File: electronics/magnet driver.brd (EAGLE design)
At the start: 101.6 x 101.6 mm, 23 parts, among them J1 1-770968-0, J2 DF1BZ-8DP-2.5DSA, K1 G2RL-2DC12, Q1 RK7002BMT116, Q2 DMN1019UVT-7DMN1019UVT-7, Q3 PMBT2222A,215PMBT2222A,215, U1 ATMEGA328PB32-TQFP

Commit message: Added pull-up on RESET
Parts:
- added R1: 10k, Zach:0805
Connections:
- net !RESET: now also R1.P$1
- net +3V3: now also R1.P$2
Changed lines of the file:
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@@
 <attribute name="NAME" x="-43.18" y="57.5936" size="0.8128" layer="25" align="bottom-center"/>
+</element>
+<element name="R1" library="Zach" package="0805" value="10k" x="-59.69" y="-2.54" smashed="yes">
+<attribute name="NAME" x="-59.69" y="-1.6764" size="0.8128" layer="25" align="bottom-center"/>
 </element>
 </elements>
@@
 <contactref element="J1" pad="3"/>
 <contactref element="J2" pad="1"/>
-<wire x1="-25.7175" y1="68.58" x2="-21.9075" y2="68.58" width="0" layer="19" extent="1-1"/>
-<wire x1="-29.5275" y1="68.58" x2="-25.7175" y2="68.58" width="0" layer="19" extent="1-1"/>
+<contactref element="R1" pad="P$2"/>
+<wire x1="-53.81" y1="13.94" x2="-58.7375" y2="-2.54" width="0" layer="19" extent="1-1"/>
+<wire x1="-53.28" y1="45.7" x2="-53.81" y2="13.94" width="0" layer="19" extent="1-1"/>
+<wire x1="-40.2045" y1="56.855" x2="-53.28" y2="45.7" width="0" layer="19" extent="1-1"/>
+<wire x1="-44.7675" y1="68.58" x2="-40.2045" y2="56.855" width="0" layer="19" extent="1-1"/>
+<wire x1="-29.5275" y1="68.58" x2="-44.7675" y2="68.58" width="0" layer="19" extent="1-1"/>
+<wire x1="-25.7175" y1="68.58" x2="-29.5275" y2="68.58" width="0" layer="19" extent="1-1"/>
+<wire x1="-21.9075" y1="68.58" x2="-25.7175" y2="68.58" width="0" layer="19" extent="1-1"/>
 <wire x1="-21.9513" y1="60.09" x2="-21.9075" y2="68.58" width="0" layer="19" extent="1-1"/>
 <wire x1="-13.6087" y1="59.29" x2="-21.9513" y2="60.09" width="0" layer="19" extent="1-1"/>
 <wire x1="-13.6087" y1="57.69" x2="-13.6087" y2="59.29" width="0" layer="19" extent="1-1"/>
-<wire x1="-44.7675" y1="68.58" x2="-29.5275" y2="68.58" width="0" layer="19" extent="1-1"/>
-<wire x1="-40.2045" y1="56.855" x2="-44.7675" y2="68.58" width="0" layer="19" extent="1-1"/>
-<wire x1="-53.28" y1="45.7" x2="-40.2045" y2="56.855" width="0" layer="19" extent="1-1"/>
-<wire x1="-53.81" y1="13.94" x2="-53.28" y2="45.7" width="0" layer="19" extent="1-1"/>
 </signal>
 <signal name="U/!D">
@@
 <contactref element="J2" pad="2"/>
 <contactref element="U1" pad="29"/>
-<wire x1="-50.78" y1="45.7" x2="-18.18" y2="63.8613" width="0" layer="19" extent="1-1"/>
+<contactref element="R1" pad="P$1"/>
+<wire x1="-50.78" y1="45.7" x2="-60.6425" y2="-2.54" width="0" layer="19" extent="1-1"/>
+<wire x1="-18.18" y1="63.8613" x2="-50.78" y2="45.7" width="0" layer="19" extent="1-1"/>
 </signal>
 <signal name="XTAL2">

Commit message: Update magnet driver.brd
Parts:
- added J3: 1-770969-0, Zach:1-770969-0
- moved J1 161.4 mm to (101.6, 36.6), turned to 90 degrees
- moved R1 131.3 mm to (64.3, 40.9), turned to 180 degrees
- moved J2 112.6 mm to (63.0, 48.3), turned to 270 degrees
- moved D2 103.9 mm to (46.2, 66.3)
- moved XTAL1 97.6 mm to (53.1, 72.1), turned to 270 degrees
- moved R2 95.8 mm to (33.0, 8.89)
- moved C7 93.1 mm to (58.7, 72.9), turned to 180 degrees
- moved C8 91.9 mm to (53.8, 68.3)
- moved C5 89.4 mm to (62.7, 70.9)
- moved C4 85.6 mm to (62.7, 68.6)
- moved C2 81.8 mm to (50.0, 21.1)
- moved U1 81.0 mm to (63.2, 61.2), turned to 270 degrees
- moved Q2 80.5 mm to (51.1, 62.2)
- moved D3 72.0 mm to (9.91, 68.3), turned to 180 degrees
- moved R3 71.3 mm to (12.7, 27.7)
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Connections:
- new net +5V: J3.2
- net +12V: now also J3.3
- net +170V: now also J3.5
- net +3V3: now also J3.1
- net GND: now also J3.4, J3.6
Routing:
- net +3V3: track 0.00 -> 149.0 mm
- net U/!D: track 0.00 -> 117.2 mm
- net +170V: track 0.00 -> 110.6 mm
- net !CS: track 0.00 -> 109.4 mm
- net +12V: track 0.00 -> 93.9 mm
- net N$8: track 0.00 -> 61.9 mm
- net N$3: track 0.00 -> 45.6 mm
- net SCL: track 0.00 -> 37.3 mm, vias 0 -> 1
- net SDA: track 0.00 -> 31.5 mm, vias 0 -> 1
- net N$2: track 0.00 -> 26.2 mm
- net N$7: track 0.00 -> 24.6 mm
- net !RESET: track 0.00 -> 24.5 mm
- net TX: track 0.00 -> 22.1 mm
- net XTAL1: track 0.00 -> 19.3 mm
- net RX: track 0.00 -> 18.5 mm
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
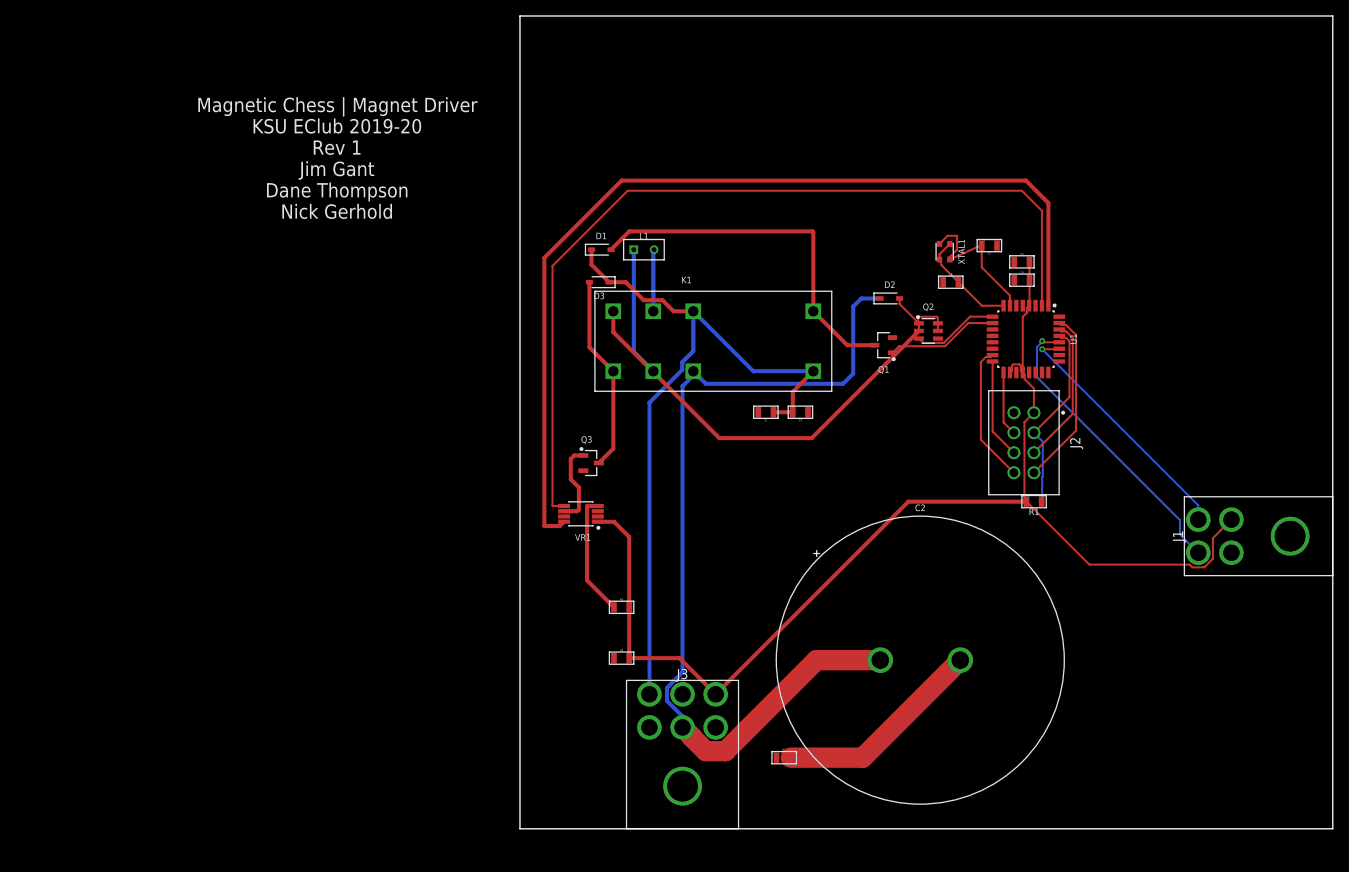
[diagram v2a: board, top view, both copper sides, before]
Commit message: Fixed some problems with the magnet driver board
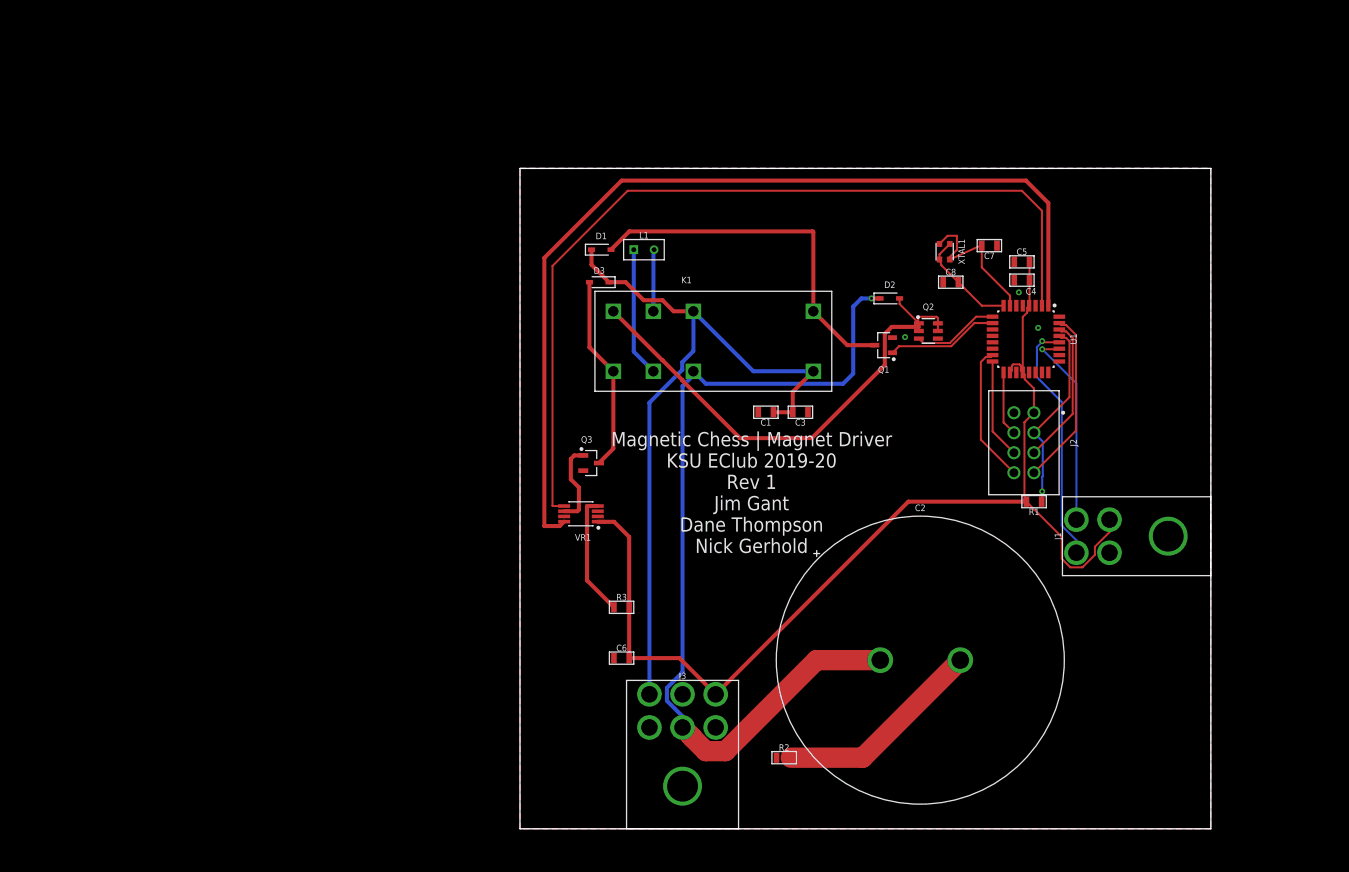
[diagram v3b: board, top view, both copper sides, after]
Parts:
- moved J1 15.2 mm to (86.4, 36.6)
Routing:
- net +3V3: track 149.0 -> 135.4 mm
- net SCL: track 37.3 -> 31.0 mm
- net SDA: track 31.5 -> 25.2 mm
- net N$8: track 61.9 -> 62.9 mm
- net !RESET: track 24.5 -> 24.0 mm, vias 0 -> 1
- net +170V: track 110.6 -> 110.7 mm, vias 0 -> 1
- added copper zone on layer 1, net GND
- added copper zone on layer 16, net GND
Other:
- board size 101.6 x 101.6 mm -> 86.4 x 82.5 mm

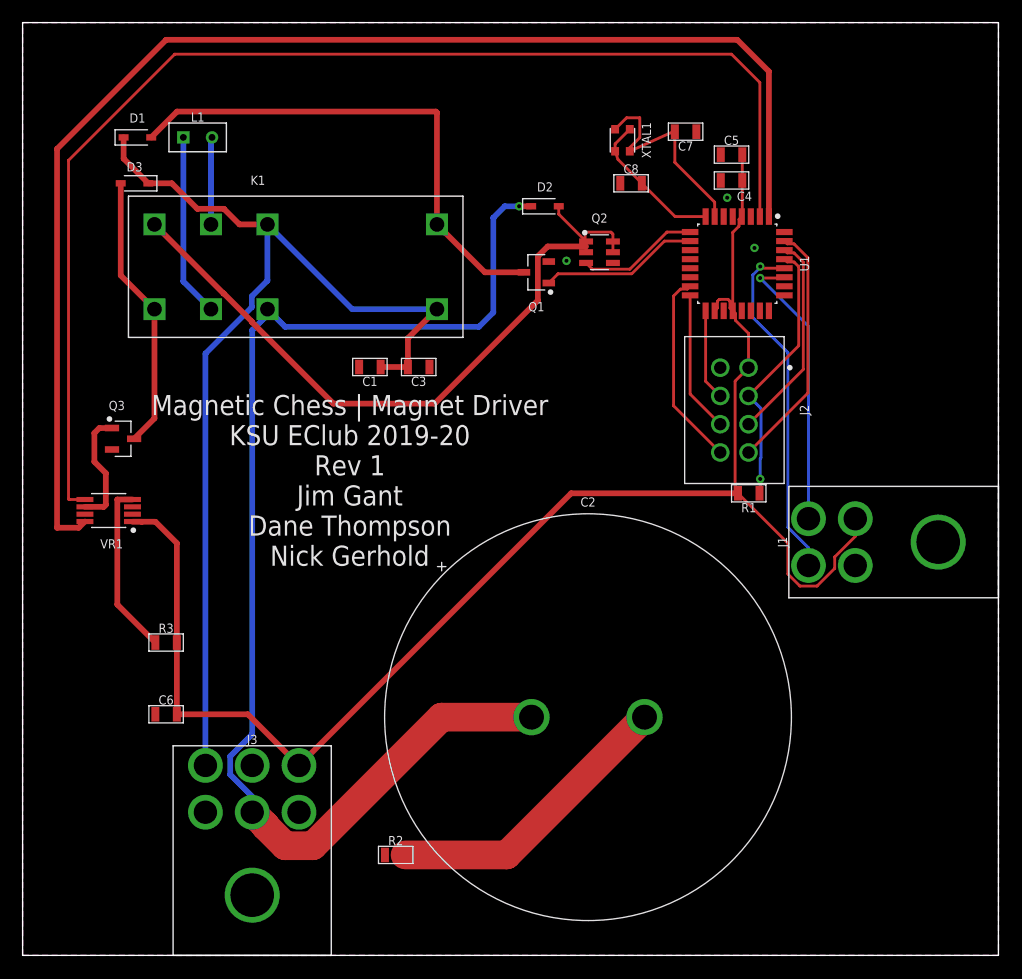
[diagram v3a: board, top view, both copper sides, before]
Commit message: Added mounting holes
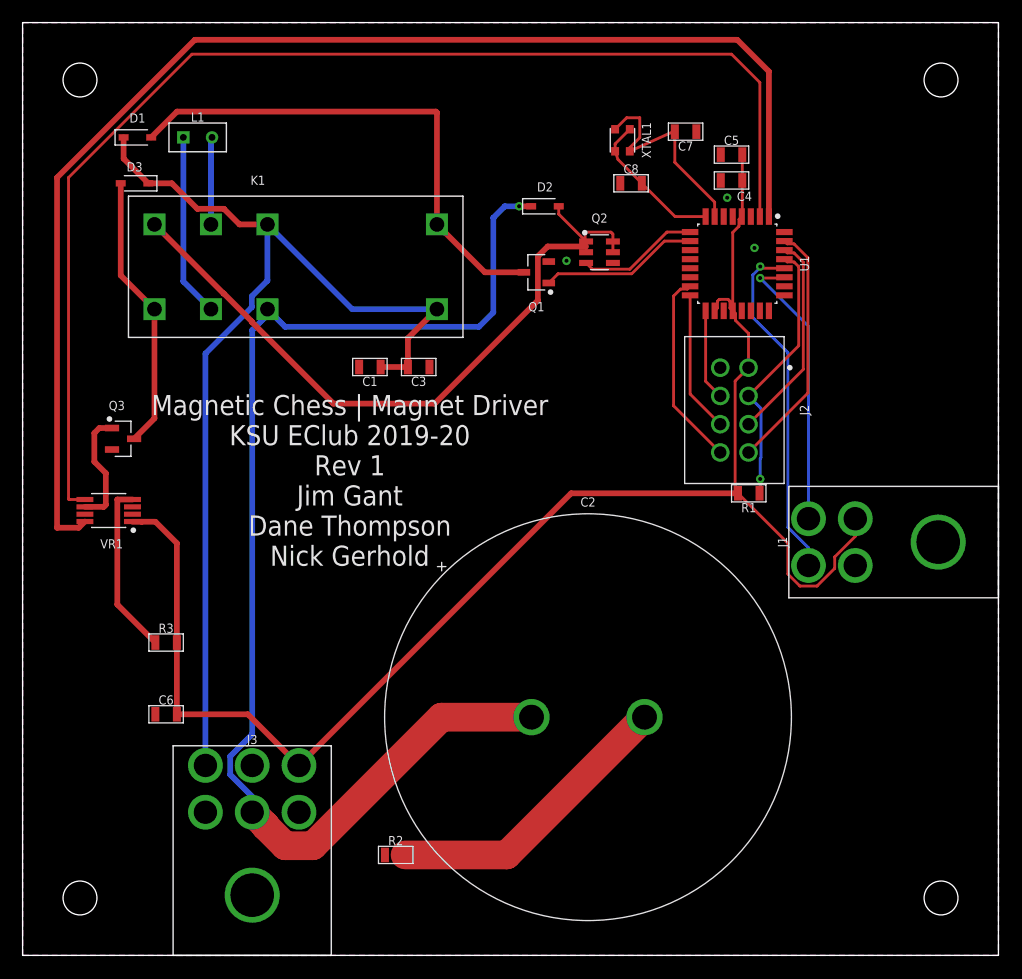
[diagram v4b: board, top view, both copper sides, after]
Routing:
- net U/!D: track 117.2 -> 115.7 mm
- net !CS: track 109.4 -> 108.5 mm
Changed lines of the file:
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@@
 <layer number="27" name="tValues" color="7" fill="1" visible="yes" active="yes"/>
 <layer number="28" name="bValues" color="7" fill="1" visible="yes" active="yes"/>
-<layer number="29" name="tStop" color="7" fill="3" visible="no" active="yes"/>
-<layer number="30" name="bStop" color="7" fill="6" visible="no" active="yes"/>
-<layer number="31" name="tCream" color="7" fill="4" visible="no" active="yes"/>
-<layer number="32" name="bCream" color="7" fill="5" visible="no" active="yes"/>
-<layer number="33" name="tFinish" color="6" fill="3" visible="no" active="yes"/>
-<layer number="34" name="bFinish" color="6" fill="6" visible="no" active="yes"/>
-<layer number="35" name="tGlue" color="7" fill="4" visible="no" active="yes"/>
-<layer number="36" name="bGlue" color="7" fill="5" visible="no" active="yes"/>
-<layer number="37" name="tTest" color="7" fill="1" visible="no" active="yes"/>
-<layer number="38" name="bTest" color="7" fill="1" visible="no" active="yes"/>
+<layer number="29" name="tStop" color="7" fill="3" visible="yes" active="yes"/>
+<layer number="30" name="bStop" color="7" fill="6" visible="yes" active="yes"/>
+<layer number="31" name="tCream" color="7" fill="4" visible="yes" active="yes"/>
+<layer number="32" name="bCream" color="7" fill="5" visible="yes" active="yes"/>
+<layer number="33" name="tFinish" color="6" fill="3" visible="yes" active="yes"/>
+<layer number="34" name="bFinish" color="6" fill="6" visible="yes" active="yes"/>
+<layer number="35" name="tGlue" color="7" fill="4" visible="yes" active="yes"/>
+<layer number="36" name="bGlue" color="7" fill="5" visible="yes" active="yes"/>
+<layer number="37" name="tTest" color="7" fill="1" visible="yes" active="yes"/>
+<layer number="38" name="bTest" color="7" fill="1" visible="yes" active="yes"/>
 <layer number="39" name="tKeepout" color="4" fill="11" visible="yes" active="yes"/>
 <layer number="40" name="bKeepout" color="1" fill="11" visible="yes" active="yes"/>
@@
 <layer number="42" name="bRestrict" color="1" fill="10" visible="yes" active="yes"/>
 <layer number="43" name="vRestrict" color="2" fill="10" visible="yes" active="yes"/>
-<layer number="44" name="Drills" color="7" fill="1" visible="no" active="yes"/>
-<layer number="45" name="Holes" color="7" fill="1" visible="no" active="yes"/>
+<layer number="44" name="Drills" color="7" fill="1" visible="yes" active="yes"/>
+<layer number="45" name="Holes" color="7" fill="1" visible="yes" active="yes"/>
 <layer number="46" name="Milling" color="3" fill="1" visible="no" active="yes"/>
 <layer number="47" name="Measures" color="7" fill="1" visible="no" active="yes"/>
@@
 Dane Thompson
 Nick Gerhold</text>
+<hole x="81.28" y="5.08" drill="3"/>
+<circle x="81.28" y="5.08" radius="4.016090625" width="0" layer="41"/>
+<circle x="81.28" y="5.08" radius="4.016090625" width="0" layer="42"/>
+<circle x="81.28" y="5.08" radius="4.016090625" width="0" layer="29"/>
+<circle x="81.28" y="5.08" radius="4.016090625" width="0" layer="30"/>
+<hole x="81.28" y="77.47" drill="3"/>
+<circle x="81.28" y="77.47" radius="4.016090625" width="0" layer="41"/>
+<circle x="81.28" y="77.47" radius="4.016090625" width="0" layer="42"/>
+<circle x="81.28" y="77.47" radius="4.016090625" width="0" layer="29"/>
+<circle x="81.28" y="77.47" radius="4.016090625" width="0" layer="30"/>
+<hole x="5.08" y="5.08" drill="3"/>
+<circle x="5.08" y="5.08" radius="4.016090625" width="0" layer="41"/>
+<circle x="5.08" y="5.08" radius="4.016090625" width="0" layer="42"/>
+<circle x="5.08" y="5.08" radius="4.016090625" width="0" layer="29"/>
+<circle x="5.08" y="5.08" radius="4.016090625" width="0" layer="30"/>
+<hole x="5.08" y="77.47" drill="3"/>
+<circle x="5.08" y="77.47" radius="4.016090625" width="0" layer="41"/>
+<circle x="5.08" y="77.47" radius="4.016090625" width="0" layer="42"/>
+<circle x="5.08" y="77.47" radius="4.016090625" width="0" layer="29"/>
+<circle x="5.08" y="77.47" radius="4.016090625" width="0" layer="30"/>
 </plain>
 <attributes>
@@
 <wire x1="5.5155" y1="38.395" x2="4.9665" y2="37.846" width="0.508" layer="1"/>
 <wire x1="4.9665" y1="37.846" x2="3.048" y2="37.846" width="0.508" layer="1"/>
-<wire x1="3.048" y1="37.846" x2="3.048" y2="71.374" width="0.508" layer="1"/>
-<wire x1="3.048" y1="71.374" x2="12.7" y2="81.026" width="0.508" layer="1"/>
+<wire x1="3.048" y1="37.846" x2="3.048" y2="68.834" width="0.508" layer="1"/>
+<wire x1="3.048" y1="68.834" x2="15.24" y2="81.026" width="0.508" layer="1"/>
 <wire x1="66.046" y1="78.226" x2="66.046" y2="65.3853" width="0.508" layer="1"/>
-<wire x1="12.7" y1="81.026" x2="63.246" y2="81.026" width="0.508" layer="1"/>
+<wire x1="15.24" y1="81.026" x2="63.246" y2="81.026" width="0.508" layer="1"/>
 <wire x1="63.246" y1="81.026" x2="66.046" y2="78.226" width="0.508" layer="1"/>
 </signal>
@@
 <contactref element="U1" pad="2"/>
 <wire x1="65.246" y1="65.3853" x2="65.246" y2="77.248" width="0.254" layer="1"/>
-<wire x1="62.738" y1="79.756" x2="13.462" y2="79.756" width="0.254" layer="1"/>
-<wire x1="13.462" y1="79.756" x2="4.064" y2="70.358" width="0.254" layer="1"/>
-<wire x1="4.064" y1="70.358" x2="4.064" y2="40.386" width="0.254" layer="1"/>
+<wire x1="62.738" y1="79.756" x2="14.986" y2="79.756" width="0.254" layer="1"/>
+<wire x1="14.986" y1="79.756" x2="4.064" y2="68.834" width="0.254" layer="1"/>
+<wire x1="4.064" y1="68.834" x2="4.064" y2="40.386" width="0.254" layer="1"/>
 <wire x1="4.064" y1="40.386" x2="4.105" y2="40.345" width="0.254" layer="1"/>
 <wire x1="4.105" y1="40.345" x2="5.5155" y2="40.345" width="0.254" layer="1"/>
